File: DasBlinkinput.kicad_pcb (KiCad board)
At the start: 4 copper layers, 25.4 x 50.8 mm, 33 parts, among them P101 CONN_01X02, P102 CONN_01X01, P103 CONN_01X01, P104 CONN_01X05, U101 LP2980, U201 MCP6404, U202 LM339

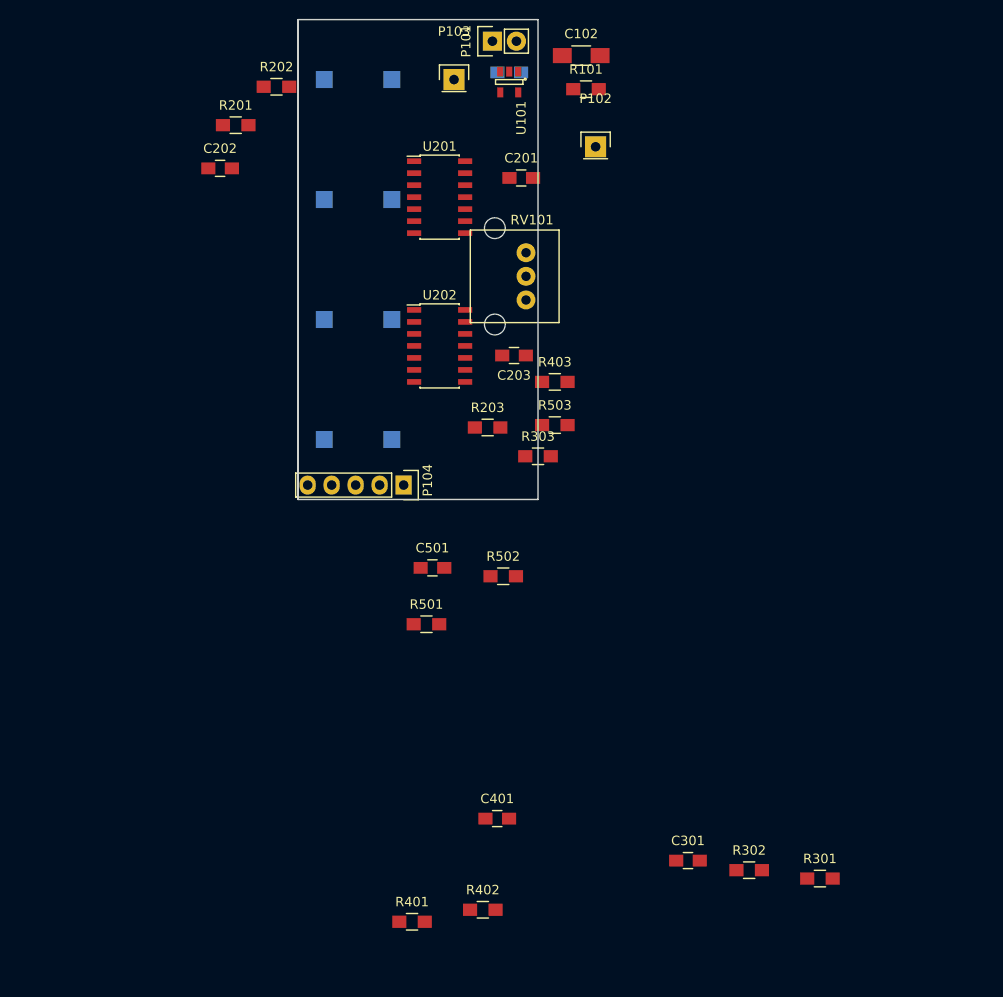
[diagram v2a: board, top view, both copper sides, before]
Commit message: removed 10K resistors used as load for op amps
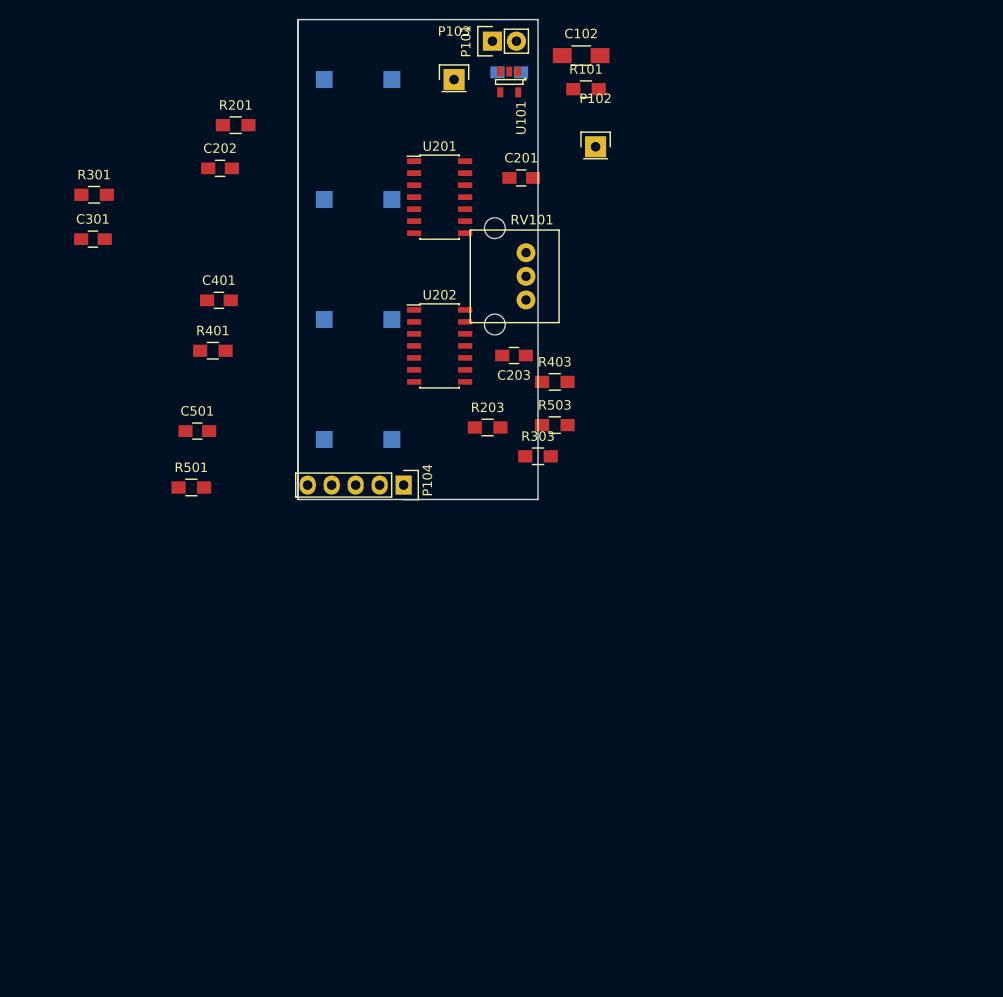
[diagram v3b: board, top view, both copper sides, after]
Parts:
- removed R202, R302, R402, R502: 10K, Resistors_SMD:R_0805_HandSoldering
- moved R301 105.6 mm to (101.6, 34.0)
- moved C301 91.1 mm to (101.5, 38.7)
- moved R401 64.0 mm to (114.2, 50.5)
- moved C401 62.3 mm to (114.8, 45.2)
- moved R501 28.8 mm to (111.9, 65.0)
- moved C501 28.8 mm to (112.5, 59.1)
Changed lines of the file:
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@@
 (kicad_pcb (version 4) (host pcbnew 4.0.2-stable)
   (general
-    (links 77)
-    (no_connects 77)
-    (area 93.205999 30.404999 195.7312 119.207)
+    (links 69)
+    (no_connects 69)
+    (area 123.114999 15.418999 148.665001 66.369001)
     (thickness 1.6)
     (drawings 5)
     (tracks 0)
     (zones 0)
-    (modules 33)
+    (modules 29)
     (nets 19)
   )
@@
   )
   (module Capacitors_SMD:C_0805_HandSoldering (layer F.Cu)
-    (at 164.465 104.521)
+    (at 101.473 38.735)
     (descr "Capacitor SMD 0805, hand soldering")
     (tags "capacitor 0805")
@@
   )
   (module Capacitors_SMD:C_0805_HandSoldering (layer F.Cu)
-    (at 144.272 100.076)
+    (at 114.808 45.212)
     (descr "Capacitor SMD 0805, hand soldering")
     (tags "capacitor 0805")
@@
   )
   (module Capacitors_SMD:C_0805_HandSoldering (layer F.Cu)
-    (at 137.414 73.533)
+    (at 112.522 59.055)
     (descr "Capacitor SMD 0805, hand soldering")
     (tags "capacitor 0805")
@@
   )
   (module Resistors_SMD:R_0805_HandSoldering (layer F.Cu)
-    (at 120.904 22.606)
-    (descr "Resistor SMD 0805, hand soldering")
-    (tags "resistor 0805")
-    (attr smd)
-    (fp_text reference R202 (at 0 -2.1) (layer F.SilkS)
-      (effects (font (size 1 1) (thickness 0.15)))
-    )
-    (fp_text value 10K (at 0 2.1) (layer F.Fab)
-      (effects (font (size 1 1) (thickness 0.15)))
-    )
-    (fp_line (start -2.4 -1) (end 2.4 -1) (layer F.CrtYd) (width 0.05))
-    (fp_line (start -2.4 1) (end 2.4 1) (layer F.CrtYd) (width 0.05))
-    (fp_line (start -2.4 -1) (end -2.4 1) (layer F.CrtYd) (width 0.05))
-    (fp_line (start 2.4 -1) (end 2.4 1) (layer F.CrtYd) (width 0.05))
-    (fp_line (start 0.6 0.875) (end -0.6 0.875) (layer F.SilkS) (width 0.15))
-    (fp_line (start -0.6 -0.875) (end 0.6 -0.875) (layer F.SilkS) (width 0.15))
-    (pad 1 smd rect (at -1.35 0) (size 1.5 1.3) (layers F.Cu F.Paste F.Mask)
-      (net 2 GND))
-    (pad 2 smd rect (at 1.35 0) (size 1.5 1.3) (layers F.Cu F.Paste F.Mask)
-      (net 4 "Net-(C202-Pad1)"))
-    (model Resistors_SMD.3dshapes/R_0805_HandSoldering.wrl
-      (at (xyz 0 0 0))
-      (scale (xyz 1 1 1))
-      (rotate (xyz 0 0 0))
-    )
-  )
-  (module Resistors_SMD:R_0805_HandSoldering (layer F.Cu)
-    (at 178.435 106.426)
+    (at 101.6 34.036)
     (descr "Resistor SMD 0805, hand soldering")
     (tags "resistor 0805")
@@
   )
   (module Resistors_SMD:R_0805_HandSoldering (layer F.Cu)
-    (at 170.942 105.537)
-    (descr "Resistor SMD 0805, hand soldering")
-    (tags "resistor 0805")
-    (attr smd)
-    (fp_text reference R302 (at 0 -2.1) (layer F.SilkS)
-      (effects (font (size 1 1) (thickness 0.15)))
-    )
-    (fp_text value 10K (at 0 2.1) (layer F.Fab)
-      (effects (font (size 1 1) (thickness 0.15)))
-    )
-    (fp_line (start -2.4 -1) (end 2.4 -1) (layer F.CrtYd) (width 0.05))
-    (fp_line (start -2.4 1) (end 2.4 1) (layer F.CrtYd) (width 0.05))
-    (fp_line (start -2.4 -1) (end -2.4 1) (layer F.CrtYd) (width 0.05))
-    (fp_line (start 2.4 -1) (end 2.4 1) (layer F.CrtYd) (width 0.05))
-    (fp_line (start 0.6 0.875) (end -0.6 0.875) (layer F.SilkS) (width 0.15))
-    (fp_line (start -0.6 -0.875) (end 0.6 -0.875) (layer F.SilkS) (width 0.15))
-    (pad 1 smd rect (at -1.35 0) (size 1.5 1.3) (layers F.Cu F.Paste F.Mask)
-      (net 2 GND))
-    (pad 2 smd rect (at 1.35 0) (size 1.5 1.3) (layers F.Cu F.Paste F.Mask)
-      (net 6 "Net-(C301-Pad1)"))
-    (model Resistors_SMD.3dshapes/R_0805_HandSoldering.wrl
-      (at (xyz 0 0 0))
-      (scale (xyz 1 1 1))
-      (rotate (xyz 0 0 0))
-    )
-  )
-  (module Resistors_SMD:R_0805_HandSoldering (layer F.Cu)
-    (at 135.255 110.998)
+    (at 114.173 50.546)
     (descr "Resistor SMD 0805, hand soldering")
     (tags "resistor 0805")
@@
   )
   (module Resistors_SMD:R_0805_HandSoldering (layer F.Cu)
-    (at 142.748 109.728)
-    (descr "Resistor SMD 0805, hand soldering")
-    (tags "resistor 0805")
-    (attr smd)
-    (fp_text reference R402 (at 0 -2.1) (layer F.SilkS)
-      (effects (font (size 1 1) (thickness 0.15)))
-    )
-    (fp_text value 10K (at 0 2.1) (layer F.Fab)
-      (effects (font (size 1 1) (thickness 0.15)))
-    )
-    (fp_line (start -2.4 -1) (end 2.4 -1) (layer F.CrtYd) (width 0.05))
-    (fp_line (start -2.4 1) (end 2.4 1) (layer F.CrtYd) (width 0.05))
-    (fp_line (start -2.4 -1) (end -2.4 1) (layer F.CrtYd) (width 0.05))
-    (fp_line (start 2.4 -1) (end 2.4 1) (layer F.CrtYd) (width 0.05))
-    (fp_line (start 0.6 0.875) (end -0.6 0.875) (layer F.SilkS) (width 0.15))
-    (fp_line (start -0.6 -0.875) (end 0.6 -0.875) (layer F.SilkS) (width 0.15))
-    (pad 1 smd rect (at -1.35 0) (size 1.5 1.3) (layers F.Cu F.Paste F.Mask)
-      (net 2 GND))
-    (pad 2 smd rect (at 1.35 0) (size 1.5 1.3) (layers F.Cu F.Paste F.Mask)
-      (net 8 "Net-(C401-Pad1)"))
-    (model Resistors_SMD.3dshapes/R_0805_HandSoldering.wrl
-      (at (xyz 0 0 0))
-      (scale (xyz 1 1 1))
-      (rotate (xyz 0 0 0))
-    )
-  )
-  (module Resistors_SMD:R_0805_HandSoldering (layer F.Cu)
-    (at 136.779 79.502)
+    (at 111.887 65.024)
     (descr "Resistor SMD 0805, hand soldering")
     (tags "resistor 0805")
@@
     (model Resistors_SMD.3dshapes/R_0805_HandSoldering.wrl
       (at (xyz 0 0 0))
-      (scale (xyz 1 1 1))
-      (rotate (xyz 0 0 0))
-    )
-  )
-  (module Resistors_SMD:R_0805_HandSoldering (layer F.Cu)
-    (at 144.907 74.422)
-    (descr "Resistor SMD 0805, hand soldering")
-    (tags "resistor 0805")
-    (attr smd)
-    (fp_text reference R502 (at 0 -2.1) (layer F.SilkS)
-      (effects (font (size 1 1) (thickness 0.15)))
-    )
-    (fp_text value 10K (at 0 2.1) (layer F.Fab)
-      (effects (font (size 1 1) (thickness 0.15)))
-    )
-    (fp_line (start -2.4 -1) (end 2.4 -1) (layer F.CrtYd) (width 0.05))
-    (fp_line (start -2.4 1) (end 2.4 1) (layer F.CrtYd) (width 0.05))
-    (fp_line (start -2.4 -1) (end -2.4 1) (layer F.CrtYd) (width 0.05))
-    (fp_line (start 2.4 -1) (end 2.4 1) (layer F.CrtYd) (width 0.05))
-    (fp_line (start 0.6 0.875) (end -0.6 0.875) (layer F.SilkS) (width 0.15))
-    (fp_line (start -0.6 -0.875) (end 0.6 -0.875) (layer F.SilkS) (width 0.15))
-    (pad 1 smd rect (at -1.35 0) (size 1.5 1.3) (layers F.Cu F.Paste F.Mask)
-      (net 2 GND))
-    (pad 2 smd rect (at 1.35 0) (size 1.5 1.3) (layers F.Cu F.Paste F.Mask)
-      (net 10 "Net-(C501-Pad1)"))
-    (model Resistors_SMD.3dshapes/R_0805_HandSoldering.wrl
-      (at (xyz 0 0 0))

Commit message: replaced potentiometer with trimpot
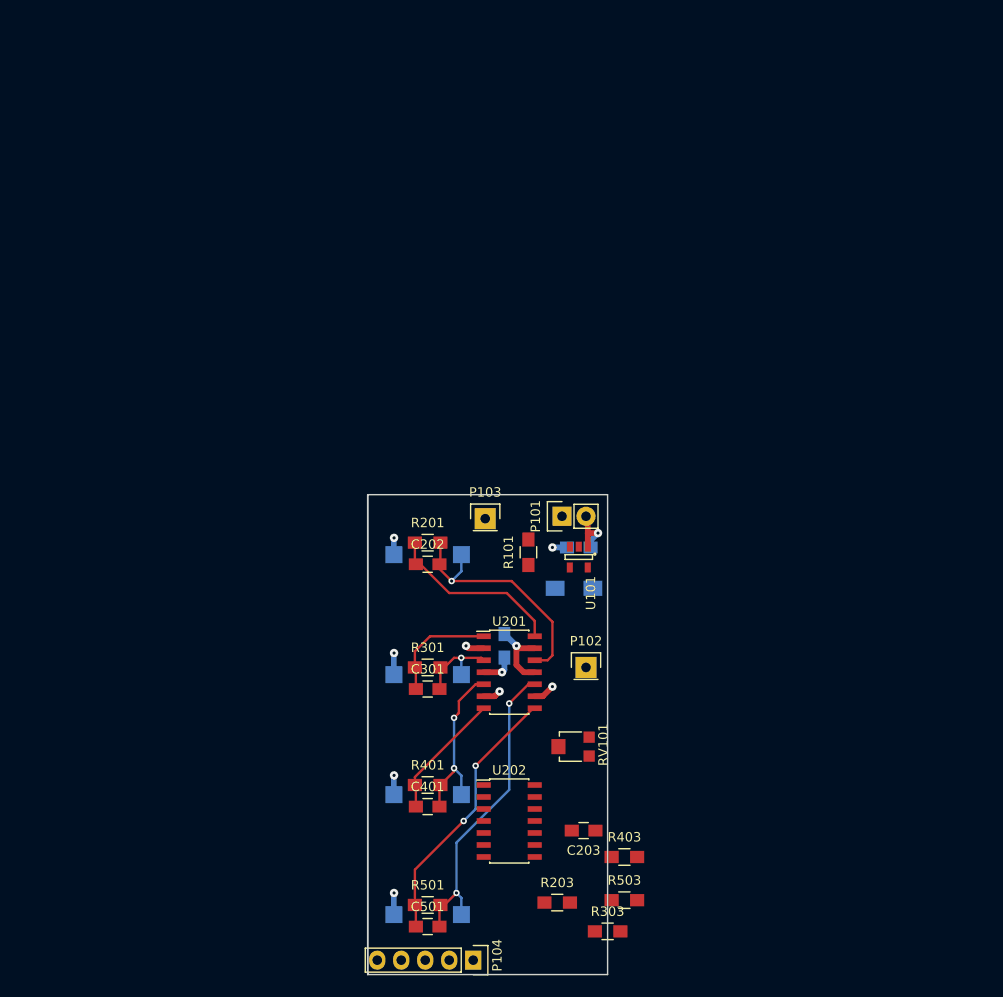
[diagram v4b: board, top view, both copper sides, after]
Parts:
- C102, C201: moved to B.Cu
- RV101: footprint DasBlinkinput:P090L-02F25BR10K -> DasBlinkinput:EVM-3YSX50B14
- moved R301 61.2 mm to (136.9, 84.1)
- moved C301 59.4 mm to (136.9, 86.4)
- moved C401 58.0 mm to (136.9, 98.8)
- moved C501 57.8 mm to (136.9, 111.5)
- moved C102 56.4 mm to (152.4, 75.7), turned to 180 degrees
- moved P102 55.1 mm to (153.7, 84.1)
- moved R401 51.3 mm to (136.9, 96.5)
- moved PD301 50.8 mm to (136.9, 84.8)
- moved PD401 50.8 mm to (136.9, 97.5)
- moved PD501 50.8 mm to (136.9, 110.2)
- moved R403 50.8 mm to (157.7, 104.1)
- moved R503 50.8 mm to (157.7, 108.7)
- moved U202 50.8 mm to (145.5, 100.3)
- moved PD201 50.8 mm to (136.9, 72.1)
- moved R203 50.8 mm to (150.6, 109.0)
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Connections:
- U201 pad 1: Net-(C202-Pad1) -> Net-(C301-Pad1)
- U201 pad 10: Net-(C401-Pad2) -> Net-(C501-Pad2)
- U201 pad 12: Net-(C501-Pad2) -> Net-(C202-Pad2)
- U201 pad 14: Net-(C501-Pad1) -> Net-(C202-Pad1)
- U201 pad 3: Net-(C202-Pad2) -> Net-(C301-Pad2)
- U201 pad 5: Net-(C301-Pad2) -> Net-(C401-Pad2)
- U201 pad 7: Net-(C301-Pad1) -> Net-(C401-Pad1)
- U201 pad 8: Net-(C401-Pad1) -> Net-(C501-Pad1)
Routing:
- net Net-(C501-Pad2): track 0.00 -> 33.0 mm, vias 0 -> 2
- net Net-(C501-Pad1): track 0.00 -> 28.5 mm, vias 0 -> 2
- net Net-(C202-Pad2): track 0.00 -> 26.0 mm, vias 0 -> 1
- net GND: track 0.00 -> 24.5 mm, vias 0 -> 9
- net Net-(C202-Pad1): track 0.00 -> 19.0 mm
- net Net-(C401-Pad2): track 0.00 -> 18.5 mm, vias 0 -> 2
- net Net-(C401-Pad1): track 0.00 -> 13.5 mm
- net Net-(C301-Pad1): track 0.00 -> 12.0 mm
- net Net-(C301-Pad2): track 0.00 -> 9.23 mm, vias 0 -> 1
- net Net-(C101-Pad1): track 0.00 -> 6.36 mm, vias 0 -> 1
- net +3V: track 0.00 -> 3.59 mm, vias 0 -> 1
- added copper zone on PWR.Cu, net +3V
- added copper zone on GND.Cu, net GND
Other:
- net class Default: clearance 0.1524 -> 0.254; trace_width 0.1524 -> 0.254
- rule trace_clearance: 0.1524 -> 0.254

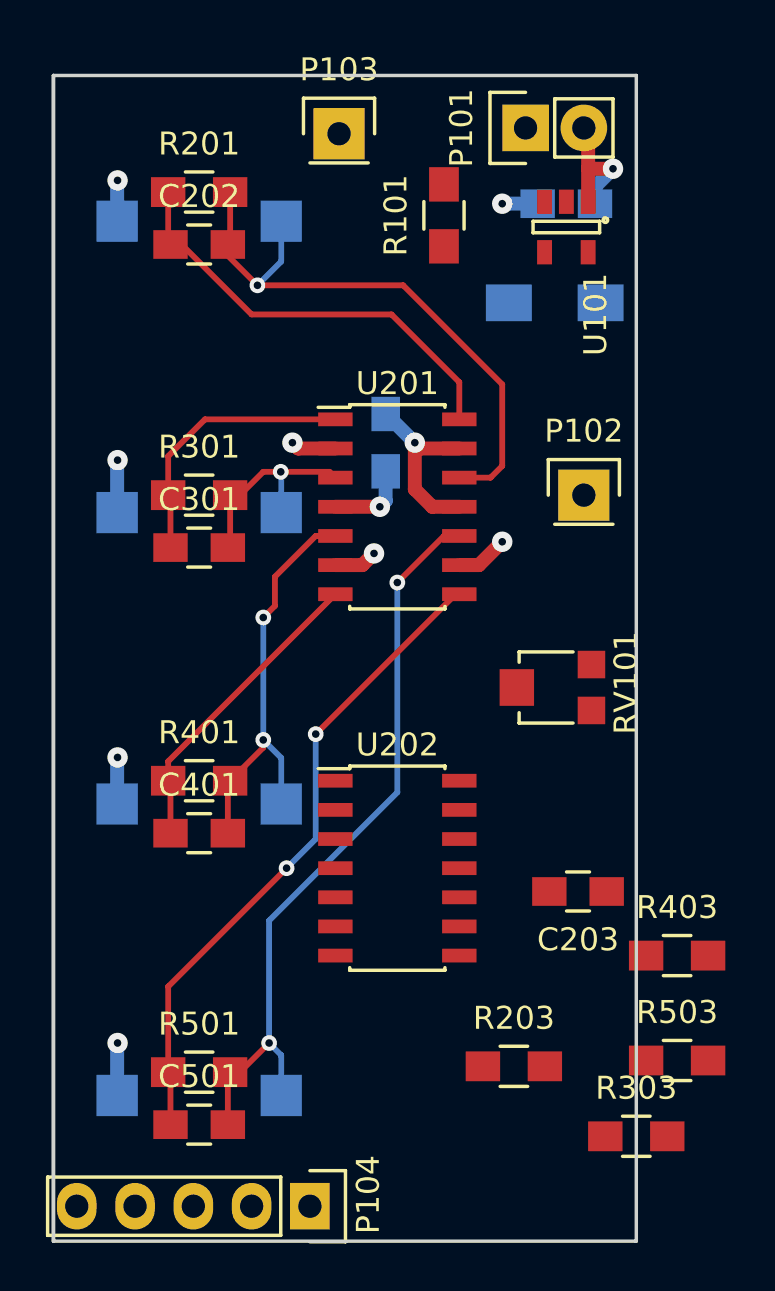
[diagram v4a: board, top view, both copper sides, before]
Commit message: completed pcb basic layout
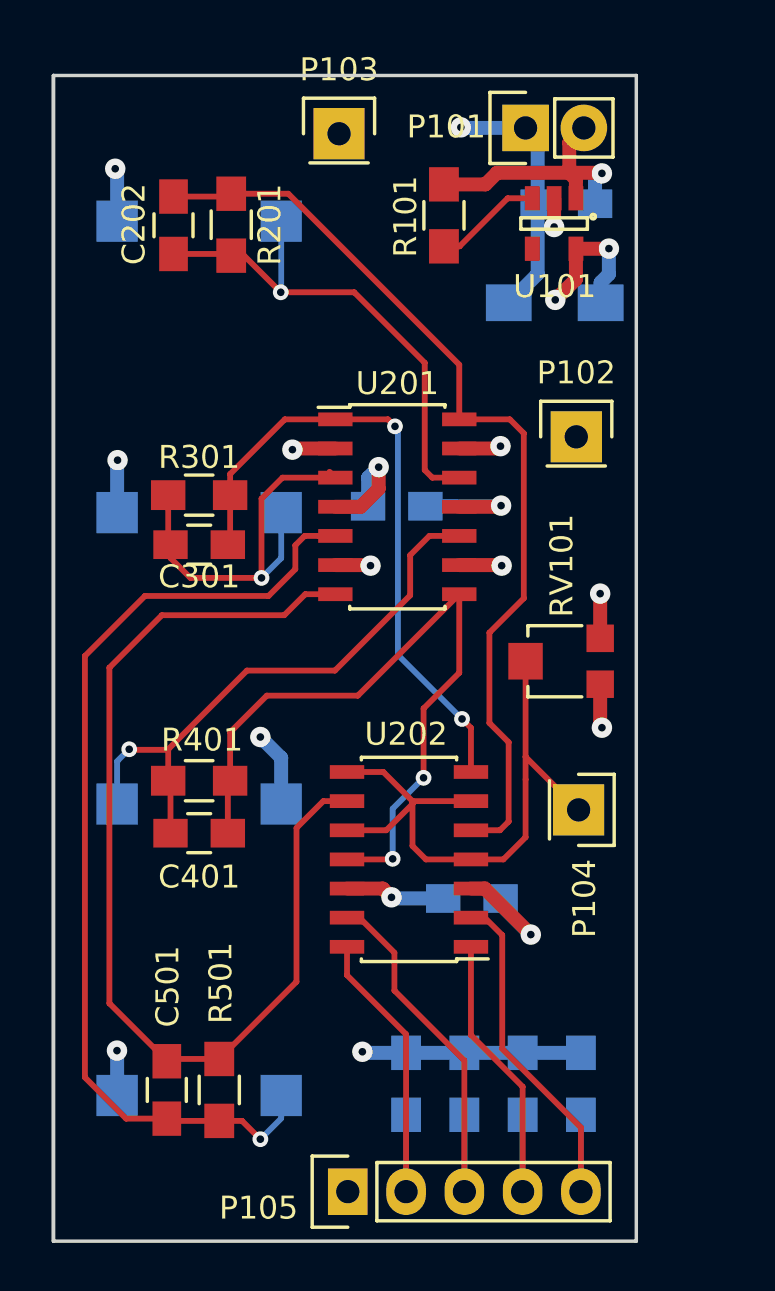
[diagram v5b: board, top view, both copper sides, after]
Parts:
- removed R203, R303, R403, R503: 10K, Resistors_SMD:R_0805_HandSoldering
- added P105: CONN_01X05, Pin_Headers:Pin_Header_Straight_1x05, F.Cu at (143.4, 114.4)
- added R202: 10K, Resistors_SMD:R_0805_HandSoldering, B.Cu at (153.5, 109.7)
- added R302: 10K, Resistors_SMD:R_0805_HandSoldering, B.Cu at (151.0, 109.7)
- added R402: 10K, Resistors_SMD:R_0805_HandSoldering, B.Cu at (148.5, 109.7)
- added R502: 10K, Resistors_SMD:R_0805_HandSoldering, B.Cu at (145.9, 109.7)
- C203: moved to B.Cu
- P104: value CONN_01X05 -> CONN_01X01; footprint Pin_Headers:Pin_Header_Straight_1x05 -> Pin_Headers:Pin_Header_Straight_1x01
- moved P104 20.9 mm to (153.4, 97.8)
- moved C203 4.63 mm to (148.8, 101.7)
- moved C201 2.81 mm to (145.5, 84.6), turned to 0 degrees
- moved P102 2.56 mm to (153.3, 81.5)
- moved C501 2.07 mm to (135.5, 110.0), turned to 270 degrees
- moved R201 1.99 mm to (138.3, 72.3), turned to 270 degrees
- moved C202 1.40 mm to (135.8, 72.3), turned to 270 degrees
- moved RV101 1.20 mm to (152.8, 91.3)
- moved R501 1.17 mm to (137.8, 110.0), turned to 270 degrees
- moved U202 0.64 mm to (146.1, 99.9), turned to 180 degrees
- moved U101 0.55 mm to (152.4, 72.2)
- moved C301 0.13 mm to (136.9, 86.2), turned to 180 degrees
- turned C401 to 180 degrees
- turned PD401 to 0 degrees
- turned R301 to 180 degrees
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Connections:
- P104 pad 1: /Channel1Photodetect/PD1 -> /Channel1Photodetect/REF_V
- U201 pad 10: Net-(C501-Pad2) -> Net-(C401-Pad2)
- U201 pad 5: Net-(C401-Pad2) -> Net-(C501-Pad2)
- U201 pad 7: Net-(C401-Pad1) -> Net-(C501-Pad1)
- U201 pad 8: Net-(C501-Pad1) -> Net-(C401-Pad1)
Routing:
- net /Channel1Photodetect/REF_V: track 0.00 -> 27.8 mm
- net +3V: track 3.59 -> 28.8 mm, vias 1 -> 6
- net Net-(C202-Pad1): track 19.0 -> 40.8 mm
- net Net-(C401-Pad1): track 13.5 -> 31.7 mm, vias 0 -> 2
- net /Channel3Photodetect/PD3: track 0.00 -> 17.7 mm
- net /Channel1Photodetect/PD1: track 0.00 -> 17.6 mm
- net Net-(C501-Pad1): track 28.5 -> 45.8 mm, vias 2 -> 0
- net Net-(C301-Pad1): track 12.0 -> 29.1 mm, vias 0 -> 2
- net GND: track 24.5 -> 40.9 mm, vias 9 -> 13
- net /Channel4Photodetect/PD4: track 0.00 -> 15.1 mm
- net /Channel2Photodetect/PD2: track 0.00 -> 15.0 mm
- net Net-(C501-Pad2): track 33.0 -> 43.8 mm, vias 2 -> 1
- net Net-(C301-Pad2): track 9.23 -> 19.0 mm
- net Net-(C401-Pad2): track 18.5 -> 26.2 mm, vias 2 -> 1
- net Net-(C101-Pad1): track 6.36 -> 12.0 mm
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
